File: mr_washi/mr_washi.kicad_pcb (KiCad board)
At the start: 2 copper layers, 147.8 x 106.3 mm, 54 parts, among them J1 PRG_01x03_Pin, J10 STATOR, J11 ROTOR, J12 TACHO, J13 Conn_01x05_Socket, J15 Conn_01x02_Socket, J16 230V_IN, J17 NTC 5k, J2 DRAIN PUMP, J3 HEATER, J4 WATER INLET 1, J5 WATER INLET 2, J6 LOW_LEVEL, J7 HIGH_LEVEL, J8 DOOR LOCK, J9 DOOR_INTERLOCK, K1 RZ03-1C4-D005, K2 RZ03-1C4-D005, K3 RZ03-1C4-D005, K4 RZ03-1C4-D005, K5 RZ03-1C4-D005, K6 RTD14730, K7 RTD14730, K8 RZ03-1C4-D005, K9 RTD14730, Q1 BTB16-600B, U1 ATtiny3226-S, U2 ULN2003, U3 MOC3020M, U4 PC817, U5 PC817, U6 MCP1825S

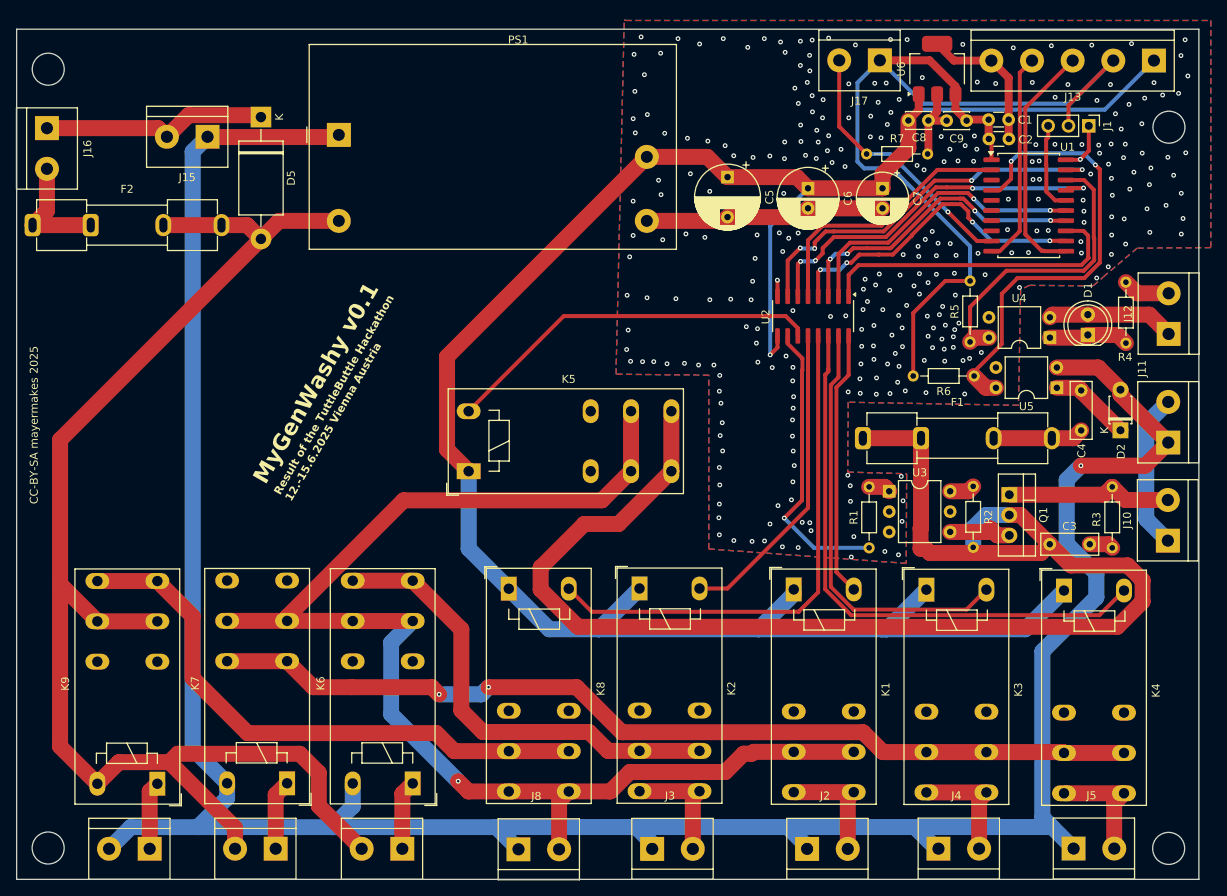
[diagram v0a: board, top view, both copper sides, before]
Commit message: updated new revision
rotated one relay, better separation of AC and 5V line,
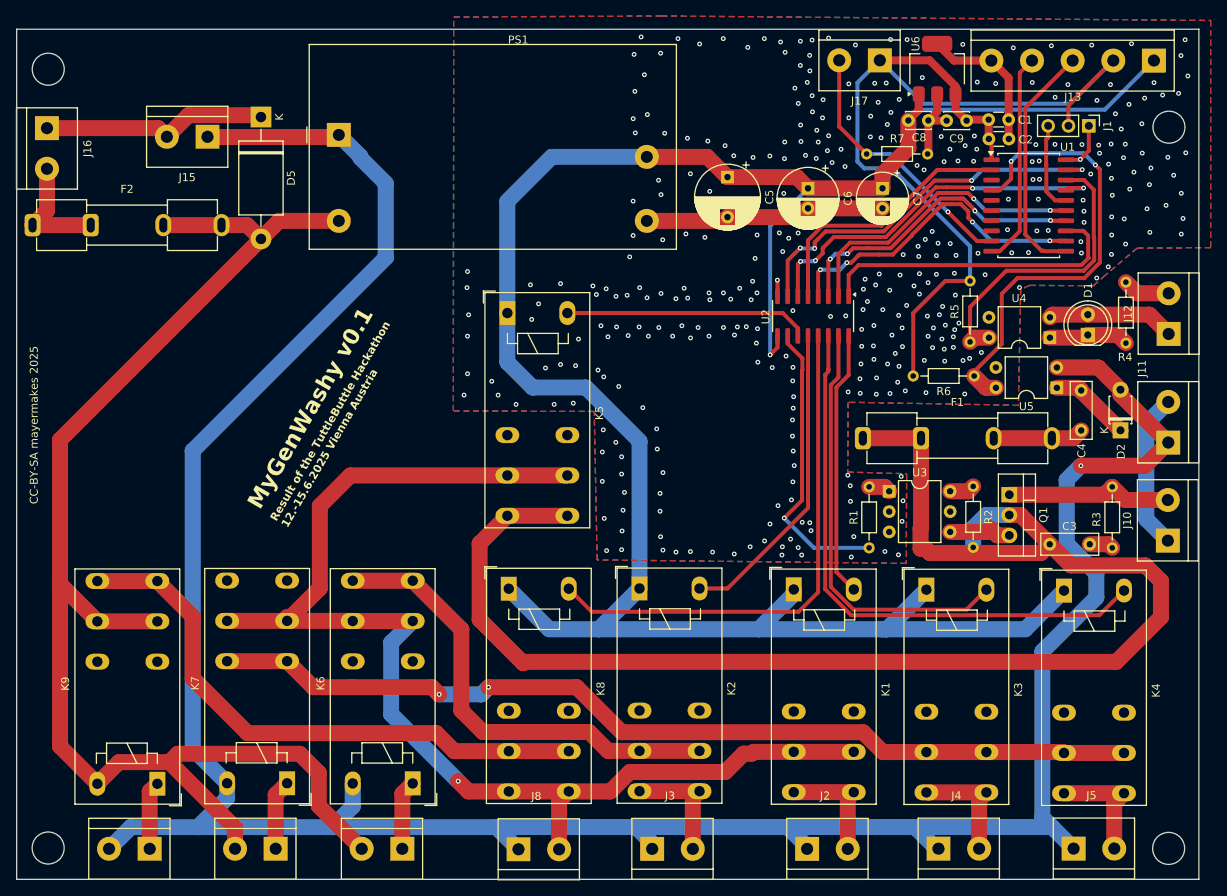
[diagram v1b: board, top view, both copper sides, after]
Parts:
- moved K5 20.4 mm to (80.6, 54.2), turned to -90 degrees
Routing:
- net Net-(U2-O6): track 47.7 -> 30.6 mm
- net 230V_NEUTRAL: track 332.6 -> 344.5 mm
- net +5V: track 266.8 -> 278.1 mm
- net /intermediary/LOCK: track 166.1 -> 156.7 mm
- net /Motor control/MOTOR_230V_LIVE: track 178.3 -> 184.2 mm
- net GND: vias 301 -> 356
